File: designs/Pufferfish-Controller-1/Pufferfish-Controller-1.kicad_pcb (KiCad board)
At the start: 6 copper layers, 216 x 127 mm, 545 parts, among them IC1 TCA9548APWR, IC2 TCA9548APWR, IC3 LMP91000SDE, IC4 W25Q16JVSSIQ, J1 TERMINAL_SCREW_4_2.54mm, J2 TERMINAL_SCREW_4_2.54mm, J3 TERMINAL_SCREW_8_2.54mm, J4 TERMINAL_SCREW_4_2.54mm, Q1 2N7002E, Q2 TP0610T

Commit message: finished component placement
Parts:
- C15, C16, C17, C18, C19, R155, R156, R157, R158, R159, R160, R161, R162, R165, R166, R167, R168, R169, R170, R171, R172, R173, R174, R175, R176, R177, R178, R179, R180, R181, R182, R183, R184, R207, R208: moved to F.Cu
- C20, C21, C25, C26, C43, C44, DRIVE1, DRIVE2, IC1, IC2, IC4, R185, R186, R187, R188, R189, R190, R191, R192, R193, R194, R195, R196, R197, R198, R199, R200, R201, R202, R203, R204, R205, R206, R209, R210, R211, R212, R213, R214, R215, R216, R217, R218, R219, R220, R221, R222, R223, R224, R225, R226, R227, R228, R229, R230, R234, R235, R238, R239, R240, R241, R244, R245, R246, R247, R249, R250, R251, R252, R253, R254, R255, R256, R260, R261, R262, R263, R265, R266, R267, R268, R269, R270, R271, R272, R277, R278, R279, R280, R282, R283, R284, R285, R286, R287, R288, R289, R290, R291, R292, R293, R294, R295, R296, R297, R298, R299, R300, R301, R302, R303, R304, R305, R306, R307, R308, R309, R310, R311, R312, R313, R314, R315, R384, R385, R386, R387, R416, R417, R418, R419, R420, R421, R422, R423, R424, R425, R426, R427: moved to B.Cu
- moved R283 178.5 mm to (305.8, 230.2), turned to 180 degrees
- moved R282 174.9 mm to (305.8, 232.2), turned to 0 degrees
- moved R278 173.3 mm to (305.8, 234.1), turned to 180 degrees
- moved CONN18 172.4 mm to (311.3, 186.9)
- moved CONN17 172.1 mm to (322.8, 186.9)
- moved CONN16 171.9 mm to (334.4, 186.9)
- moved R277 170.4 mm to (305.8, 236.1), turned to 0 degrees
- moved R270 168.7 mm to (305.8, 238.0), turned to 180 degrees
- moved R299 165.7 mm to (291.1, 189.1)
- moved R315 165.7 mm to (303.8, 189.1)
- moved R269 165.4 mm to (305.8, 239.9), turned to 0 degrees
- moved R266 164.1 mm to (305.8, 241.9), turned to 180 degrees
- moved R298 162.1 mm to (291.1, 191.0)
- moved R314 162.1 mm to (303.8, 191.0)
- moved R265 160.4 mm to (305.8, 243.8), turned to 0 degrees
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
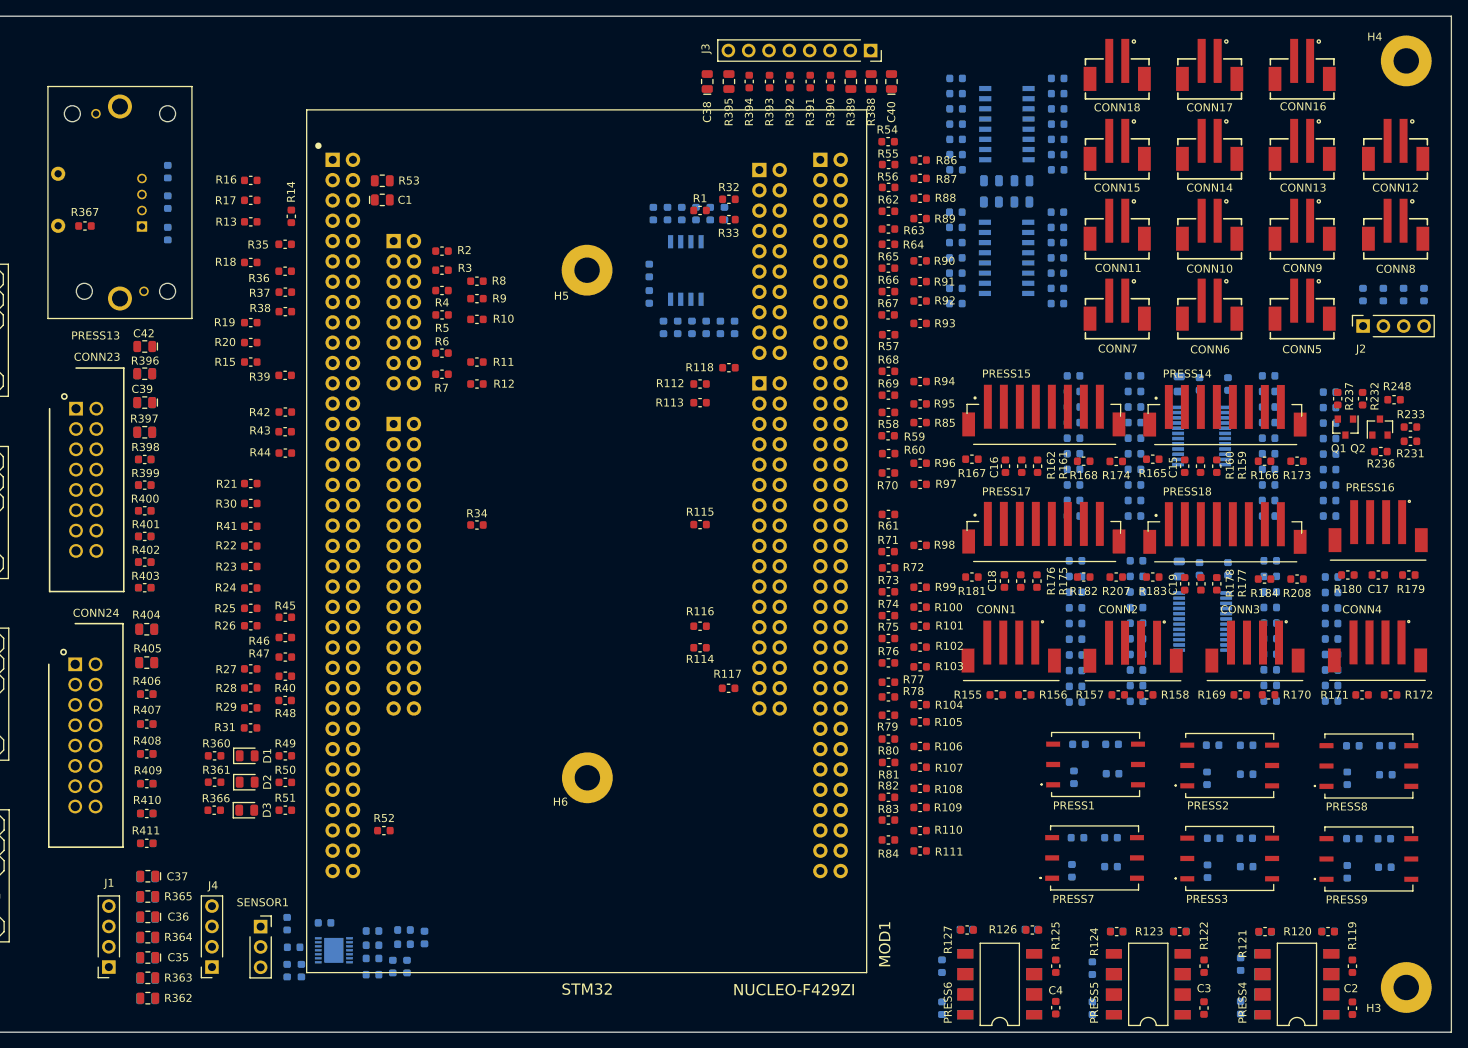
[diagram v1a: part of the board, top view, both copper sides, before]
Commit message: added ground and power planes
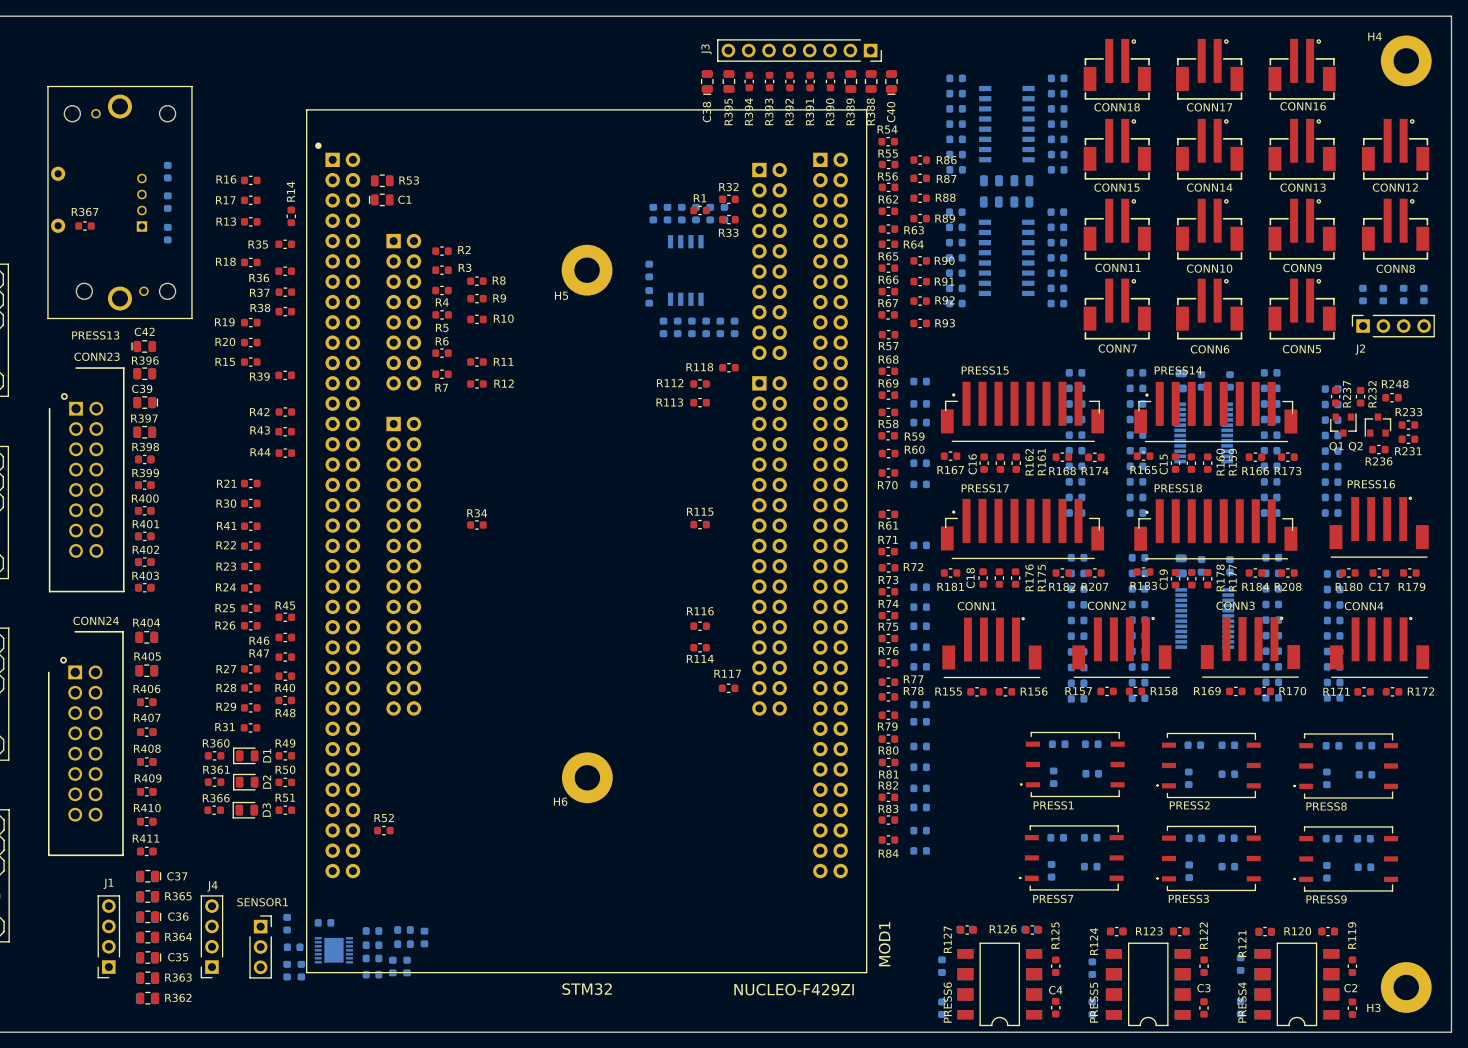
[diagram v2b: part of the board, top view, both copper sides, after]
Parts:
- R100, R101, R102, R103, R104, R105, R106, R107, R108, R109, R110, R111, R85, R94, R95, R96, R97, R98, R99: moved to B.Cu
- moved R168 2.71 mm to (304.4, 236.5)
- moved R182 2.71 mm to (304.4, 251.0)
- moved R181 2.71 mm to (290.4, 251.0)
- moved R207 2.71 mm to (308.5, 251.0)
- moved R174 2.71 mm to (308.5, 236.5)
- moved C16 2.69 mm to (294.6, 237.2)
- moved C18 2.69 mm to (294.5, 251.6)
- moved PRESS15 2.69 mm to (298.4, 232.3)
- moved PRESS17 2.69 mm to (298.4, 246.9)
- moved R175 2.69 mm to (298.6, 251.6)
- moved R161 2.69 mm to (298.7, 237.2)
- moved R162 2.69 mm to (296.7, 237.2)
- moved R167 2.69 mm to (290.4, 236.3)
- moved R176 2.69 mm to (296.5, 251.6)
- moved C11 2.54 mm to (303.1, 288.2)
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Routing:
- added copper zone on In4.Cu, net 12V
- added copper zone on In4.Cu, net 3.3V
- added copper zone on In4.Cu, net 5V
- added copper zone on In1.Cu, net GND

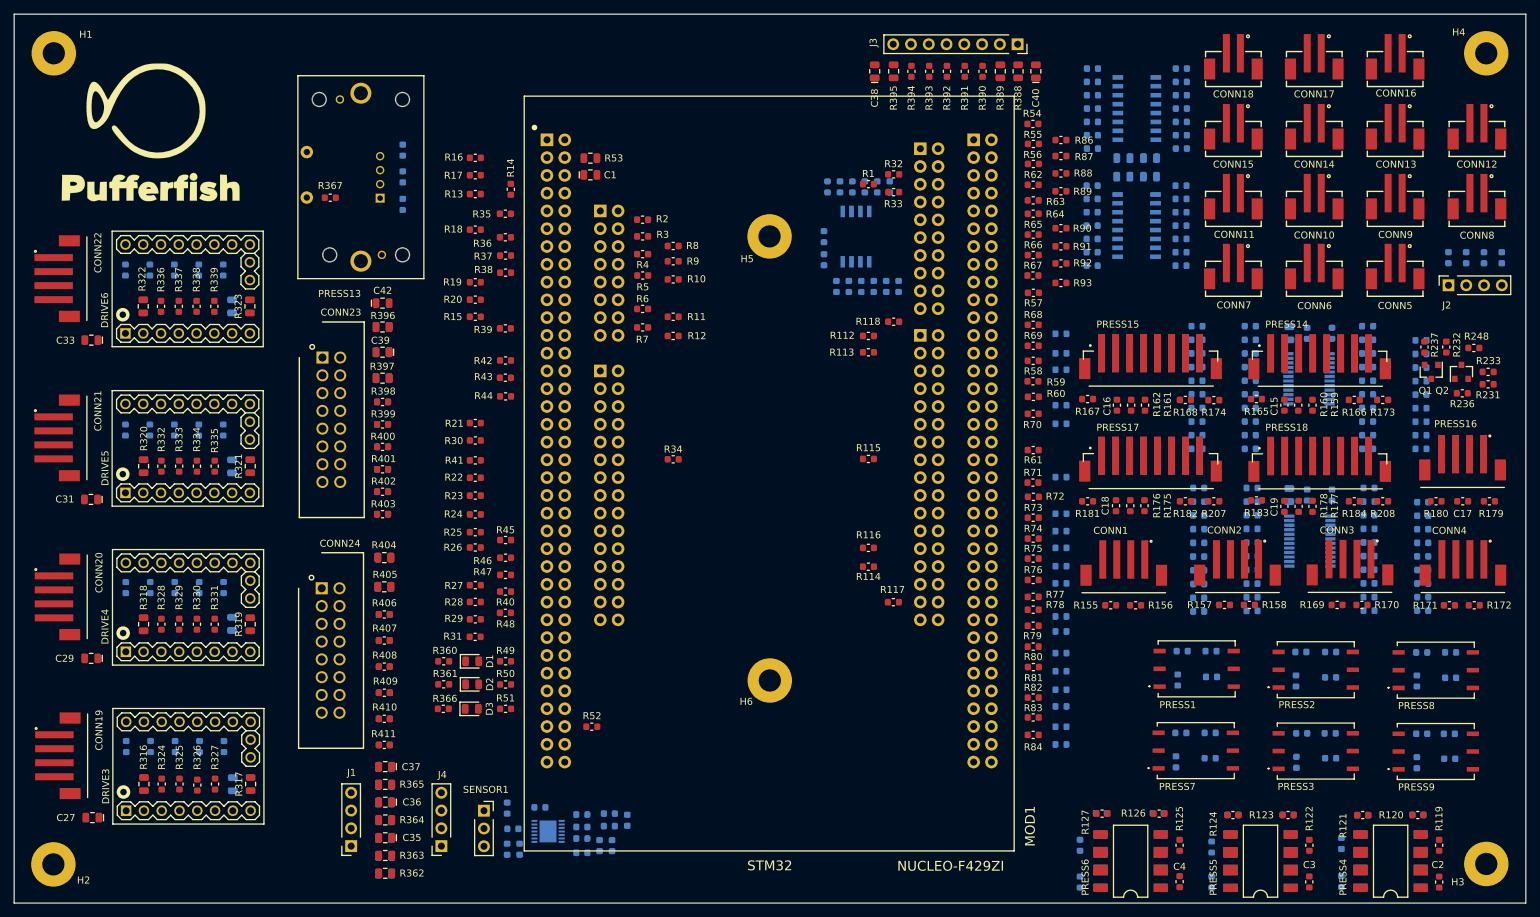
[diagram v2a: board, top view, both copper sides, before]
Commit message: autorouted traces using FreeRouting.jar
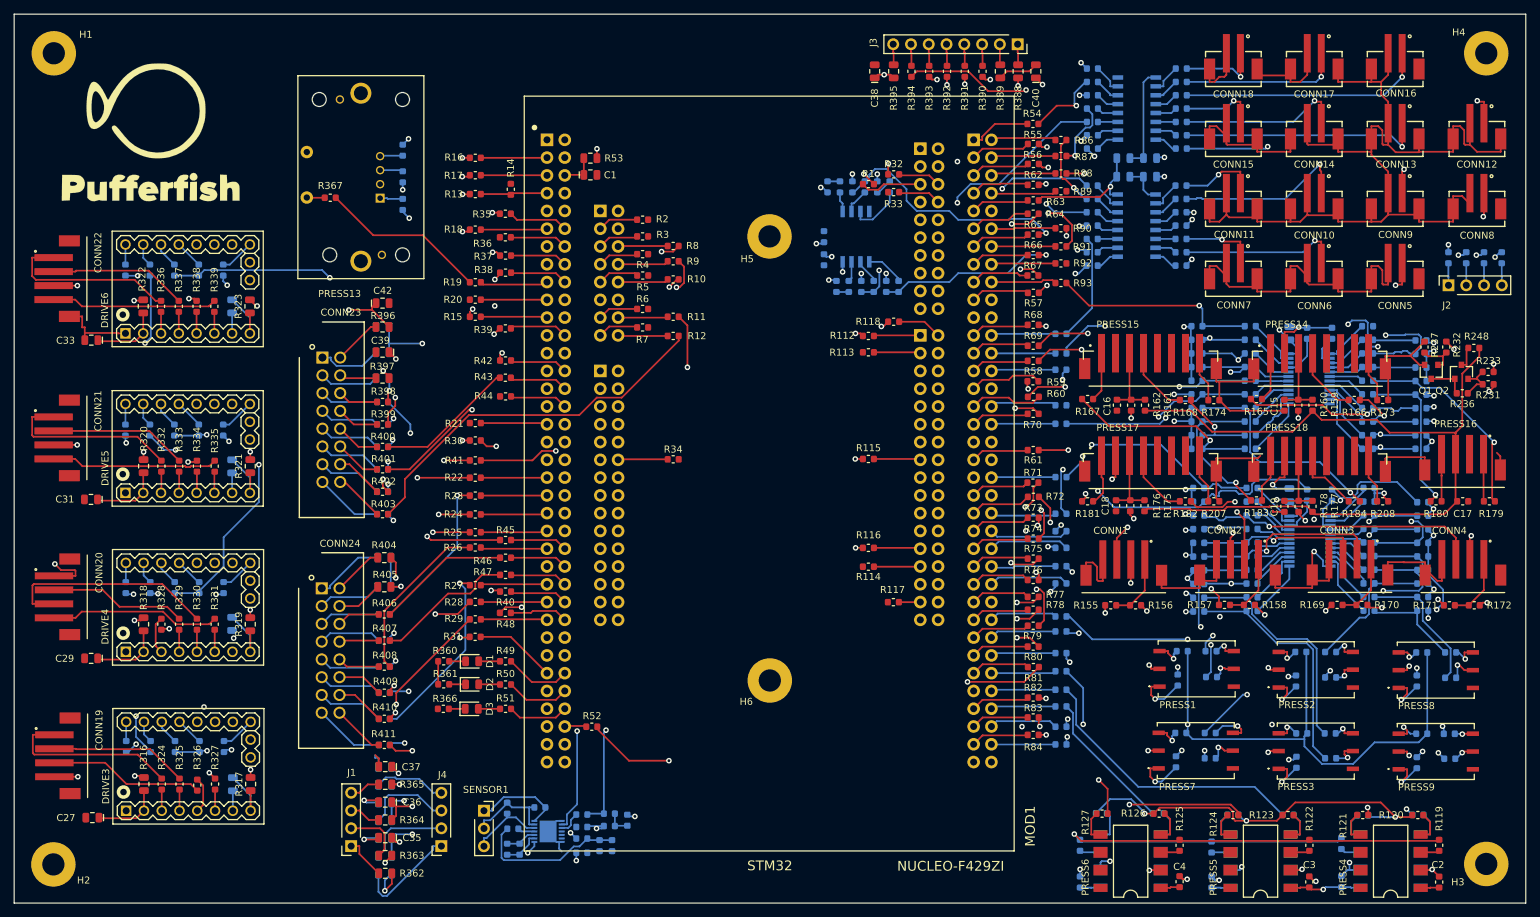
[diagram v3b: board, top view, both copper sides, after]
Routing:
- net GND: track 0.00 -> 546.1 mm, vias 0 -> 18
- net SPI1_MISO: track 0.00 -> 215.5 mm, vias 0 -> 2
- net MOTOR4_DIR: track 0.00 -> 189.6 mm, vias 0 -> 3
- net SPI1_SCL: track 0.00 -> 180.9 mm, vias 0 -> 5
- net MOTOR4_STEP: track 0.00 -> 176.4 mm, vias 0 -> 3
- net I2C1_SD0: track 0.00 -> 175.0 mm, vias 0 -> 2
- net MOTOR4_EN: track 0.00 -> 169.8 mm, vias 0 -> 3
- net PRESSX_EN: track 0.00 -> 166.1 mm, vias 0 -> 2
- net I2C1_SC0: track 0.00 -> 164.0 mm, vias 0 -> 2
- net MOTOR1_DIR: track 0.00 -> 159.5 mm, vias 0 -> 2
- net MOTOR1_STEP: track 0.00 -> 155.5 mm, vias 0 -> 2
- net 5V: track 0.00 -> 153.1 mm, vias 0 -> 20
- net 3.3V: track 0.00 -> 149.9 mm, vias 0 -> 77
- net MOTOR2_DIR: track 0.00 -> 139.6 mm, vias 0 -> 2
- net MOTOR2_STEP: track 0.00 -> 136.7 mm, vias 0 -> 2
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
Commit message: touched up routing and layed out power planes
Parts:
- added R428: SHORT_SMD_0603, Pufferfish:SHORT_SMD_0603, B.Cu at (165.0, 279.4)
- added R429: SHORT_SMD_0603, Pufferfish:SHORT_SMD_0603, B.Cu at (169.3, 279.4)
- added R430: SHORT_SMD_0603, Pufferfish:SHORT_SMD_0603, B.Cu at (165.0, 256.7)
- added R431: SHORT_SMD_0603, Pufferfish:SHORT_SMD_0603, B.Cu at (169.3, 256.7)
- added R432: SHORT_SMD_0603, Pufferfish:SHORT_SMD_0603, B.Cu at (164.7, 233.9)
- added R433: SHORT_SMD_0603, Pufferfish:SHORT_SMD_0603, B.Cu at (169.0, 233.9)
- added R434: SHORT_SMD_0603, Pufferfish:SHORT_SMD_0603, B.Cu at (164.8, 211.2)
- added R435: SHORT_SMD_0603, Pufferfish:SHORT_SMD_0603, B.Cu at (169.2, 211.2)
- moved L1 0.44 mm to (156.6, 197.7)
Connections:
- DRIVE3 pad 14: (no net) -> Net-(DRIVE3-Pad14)
- DRIVE3 pad 15: (no net) -> Net-(DRIVE3-Pad15)
- DRIVE4 pad 14: (no net) -> Net-(DRIVE4-Pad14)
- DRIVE4 pad 15: (no net) -> Net-(DRIVE4-Pad15)
- DRIVE5 pad 14: (no net) -> Net-(DRIVE5-Pad14)
- DRIVE5 pad 15: (no net) -> Net-(DRIVE5-Pad15)
- DRIVE6 pad 14: (no net) -> Net-(DRIVE6-Pad14)
- DRIVE6 pad 15: (no net) -> Net-(DRIVE6-Pad15)
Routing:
- net GND: track 546.1 -> 696.4 mm, vias 18 -> 105
- net Net-(C24-Pad1): track 21.8 -> 29.8 mm
- net CPU_UART_RX: track 55.4 -> 61.8 mm, vias 2 -> 3
- net MOTOR3_UART: track 74.8 -> 80.8 mm
- net 5V: track 153.1 -> 147.0 mm, vias 20 -> 18
- net I2C2_SDA: track 68.9 -> 63.4 mm, vias 2 -> 3
- net 12V: track 28.9 -> 33.9 mm, vias 11 -> 42
- net CPU_UART_CLK: track 54.0 -> 49.3 mm, vias 2 -> 0
- net 3.3V: track 149.9 -> 154.1 mm
- net SPI1_SCL: track 180.9 -> 184.9 mm, vias 5 -> 8
- net Net-(DRIVE5-Pad15): track 0.00 -> 3.89 mm
- net Net-(DRIVE4-Pad14): track 0.00 -> 3.84 mm
- net Net-(DRIVE6-Pad15): track 0.00 -> 3.84 mm
- net Net-(DRIVE3-Pad15): track 0.00 -> 3.80 mm
- net Net-(DRIVE6-Pad14): track 0.00 -> 3.72 mm
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- added copper zone on B.Cu, net 12V
- added copper zone on In4.Cu, net GND

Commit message: completed PCB layout
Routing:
- net Net-(J1-Pad2): track 8.61 -> 5.39 mm
- net Net-(J4-Pad3): track 13.1 -> 10.5 mm
- net GND: track 696.4 -> 694.8 mm
- net 12V: track 33.9 -> 35.0 mm
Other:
- board text added: "PezGlobo Pufferfish Controller v1.0 Chris Arcadia (2020/06/23)"

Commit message: moved one of the unused GPIO pins from the jumper to the interface board connector
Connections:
- R387 pad 2: GPIO4 -> GND
- R398 pad 1: GND -> GPIO4
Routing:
- net GPIO4: track 85.8 -> 104.8 mm, vias 2 -> 1
- net GND: track 694.8 -> 694.9 mm, vias 105 -> 106

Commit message: minor pcb updates and folder organization
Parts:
- moved C27 0.25 mm to (148.3, 296.4)
- moved DRIVE6 0.15 mm to (176.5, 221.1)
- moved DRIVE3 0.14 mm to (176.7, 289.6)
- moved DRIVE5 0.08 mm to (176.5, 244.0)
- renumbered R428 to R344, R429 to R345, R344 to R346, R345 to R347, R346 to R348, R347 to R349, R348 to R350, R430 to R351, R431 to R352, R349 to R353, R350 to R354, R351 to R355, R352 to R356, R353 to R357, R432 to R358, R433 to R359, R354 to R360, R355 to R361, R356 to R362, R357 to R363, R358 to R364, R434 to R365, R435 to R366, R359 to R367, R360 to R368, R361 to R369, R362 to R370, R363 to R371, R364 to R372, R365 to R373, R366 to R374, R367 to R375, R368 to R376, R369 to R377, R370 to R378, R371 to R379, R372 to R380, R373 to R381, R374 to R382, R375 to R383, R376 to R384, R377 to R385, R378 to R386, R379 to R387, R380 to R388, R381 to R389, R382 to R390, R383 to R391, R384 to R392, R385 to R393, R386 to R394, R387 to R395, R388 to R396, R389 to R397, R390 to R398, R391 to R399, R392 to R400, R393 to R401, R394 to R402, R395 to R403, R396 to R404, R397 to R405, R398 to R406, R399 to R407, R400 to R408, R401 to R409, R402 to R410, R403 to R411, R404 to R412, R405 to R413, R406 to R414, R407 to R415, R408 to R416, R409 to R417, R410 to R418, R411 to R419, R412 to R420, R413 to R421, R414 to R422, R415 to R423, R416 to R424, R417 to R425, R418 to R426, R419 to R427, R420 to R428, R421 to R429, R422 to R430, R423 to R431, R424 to R432, R425 to R433, R426 to R434, R427 to R435
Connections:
- net GPIO4 renamed SET_EXTRA
- net LEDY_EN renamed LEDB_EN
- net SET_NOT_PAUSE renamed SET_LOCK
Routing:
- net MOTOR1_STEP: track 155.5 -> 156.5 mm
- net MOTOR1_DIR: track 160.6 -> 161.5 mm
- net 5V: track 147.4 -> 148.2 mm
- net Net-(C27-Pad1): track 9.79 -> 10.5 mm
- net MOTOR2_UART: track 63.9 -> 64.4 mm
- added copper zone on In2.Cu, net 12V
- removed copper zone on B.Cu, net 12V
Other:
- board text added: "Pez Globo Pufferfish Controller v1.0 Chris3Arcadia (2020/06/29)"
- board text removed: "PezGlobo Pufferfish Controller v1.0 Chris Arcadia (2020/06/23)"
